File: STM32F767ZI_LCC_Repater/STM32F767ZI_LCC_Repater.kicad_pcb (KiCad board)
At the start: 2 copper layers, 105.6 x 73.3 mm, 6 parts, among them CN10 ST_MORPHO, CN7 ST_MORPHO

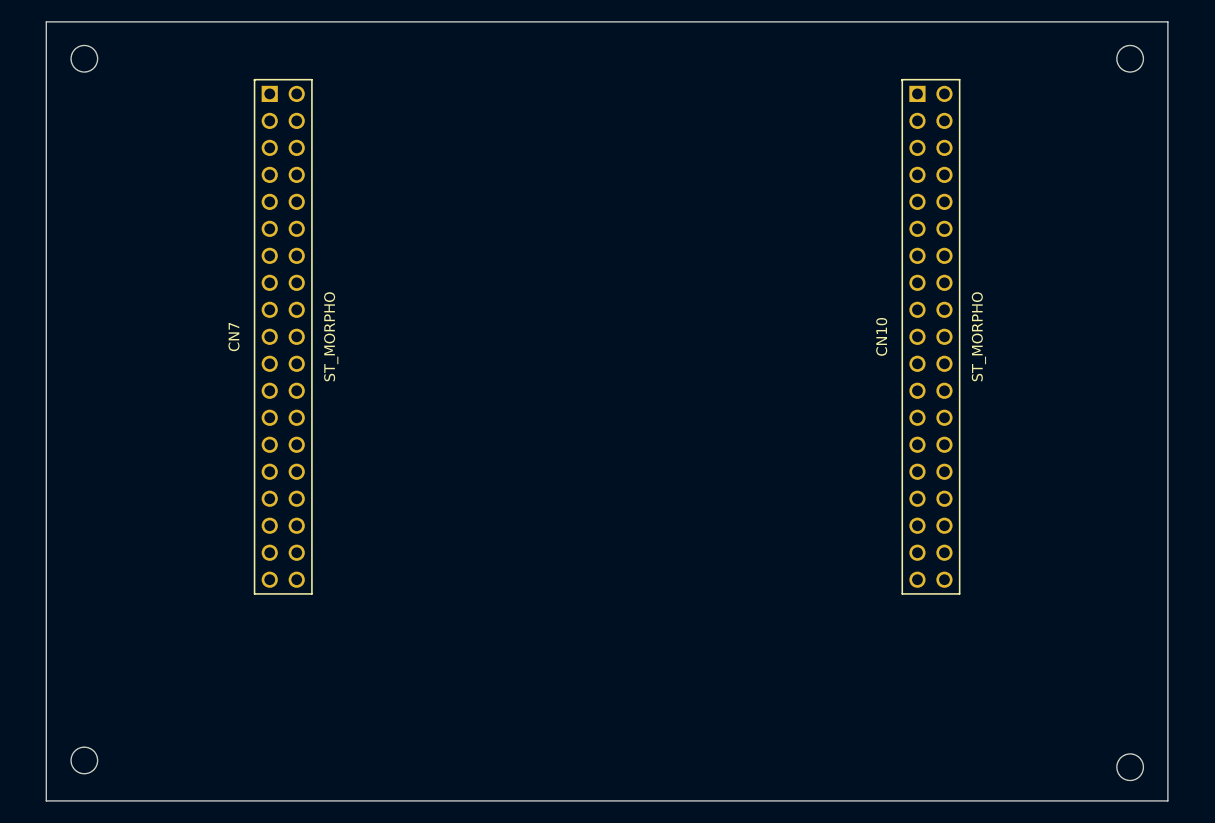
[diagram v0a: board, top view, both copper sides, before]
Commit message: Complete STM32F767ZI_LCC_Repater board.
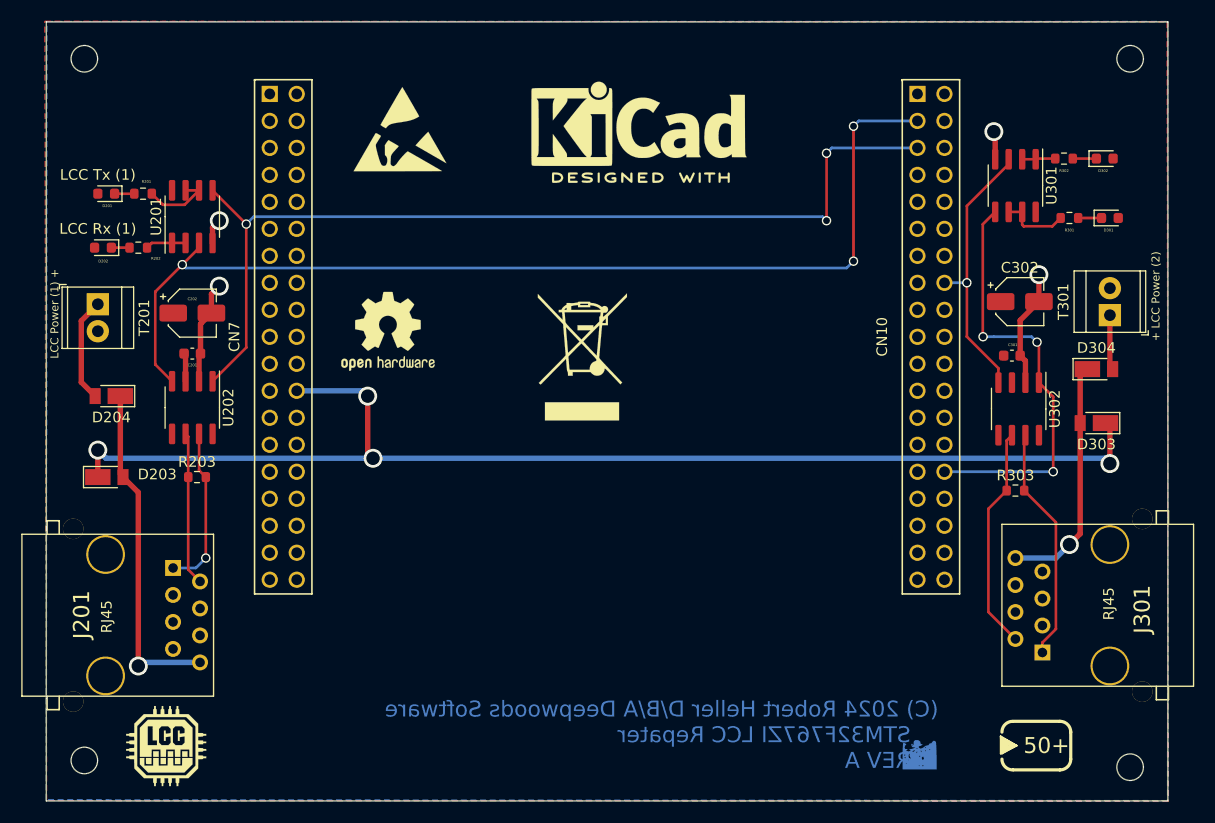
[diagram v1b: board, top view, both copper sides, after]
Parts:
- added C201: .1 uf, Capacitor_SMD:C_0603_1608Metric, F.Cu at (92.7, 191.6)
- added C202: 15 uf 15V, Capacitor_SMD:CP_Elec_4x5.8, F.Cu at (92.7, 187.8)
- added C301: .1 uf, Capacitor_SMD:C_0603_1608Metric, F.Cu at (169.8, 191.8)
- added C302: 15 uf 15V, Capacitor_SMD:CP_Elec_4x5.8, F.Cu at (170.6, 186.7)
- added D201: LCC Tx (1), LED_SMD:LED_0603_1608Metric, F.Cu at (84.6, 176.5)
- added D202: LCC Rx (1), LED_SMD:LED_0603_1608Metric, F.Cu at (84.3, 181.6)
- added D203: SB240, Diode_SMD:D_PowerDI-123, F.Cu at (84.7, 203.2)
- added D204: SB240, Diode_SMD:D_PowerDI-123, F.Cu at (85.1, 195.6)
- added D301: LCC Tx (2), LED_SMD:LED_0603_1608Metric, F.Cu at (179.1, 178.8)
- added D302: LCC Rx (2), LED_SMD:LED_0603_1608Metric, F.Cu at (178.6, 173.2)
- added D303: SB240, Diode_SMD:D_PowerDI-123, F.Cu at (177.8, 198.1)
- added D304: SB240, Diode_SMD:D_PowerDI-123, F.Cu at (177.8, 193.0)
- added G***: LCC, LCCLogo:LCC_LOGO_9x9, F.Cu at (90.3, 228.5)
- added G***: LOGO, DWSLogos:DWSLogoBCU, F.Cu at (161.2, 229.1)
- added J201: RJ45, RJ45:RJ45_8N-S, F.Cu at (84.5, 216.2)
- added J301: RJ45, RJ45:RJ45_8N-S, F.Cu at (179.1, 215.3)
- added R201: 160 Ohms, Resistor_SMD:R_0603_1608Metric, F.Cu at (88.1, 176.5)
- added R202: 160 Ohms, Resistor_SMD:R_0603_1608Metric, F.Cu at (87.6, 181.6)
- added R203: 120, Resistor_SMD:R_0603_1608Metric, F.Cu at (93.2, 203.2)
- added R301: 160 Ohms, Resistor_SMD:R_0603_1608Metric, F.Cu at (175.3, 178.8)
- added R302: 160 Ohms, Resistor_SMD:R_0603_1608Metric, F.Cu at (174.8, 173.2)
- added R303: 120, Resistor_SMD:R_0603_1608Metric, F.Cu at (170.2, 204.5)
- added REF**: ESD-Logo_8.9x8mm_SilkScreen, Symbol:ESD-Logo_8.9x8mm_SilkScreen, F.Cu at (112.3, 170.4)
- added REF**: WEEE-Logo_8.4x12mm_SilkScreen, Symbol:WEEE-Logo_8.4x12mm_SilkScreen, F.Cu at (129.4, 191.9)
- added REF**: KiCad-Logo2_8mm_SilkScreen, Symbol:KiCad-Logo2_8mm_SilkScreen, F.Cu at (134.7, 169.9)
- added REF**: OSHW-Logo2_9.8x8mm_SilkScreen, Symbol:OSHW-Logo2_9.8x8mm_SilkScreen, F.Cu at (111.1, 189.5)
- added REF**: PowerLabel-50Plus, PowerLabels:PowerLabel-50Plus, F.Cu at (173.1, 228.5)
- added T201: LCC Power (1) +, TerminalBlock_TE-Connectivity:TerminalBlock_TE_282834-2_1x02_P2.54mm_Horizontal, F.Cu at (83.8, 186.9)
- added T301: + LCC Power (2), TerminalBlock_TE-Connectivity:TerminalBlock_TE_282834-2_1x02_P2.54mm_Horizontal, F.Cu at (179.1, 188.0)
- added U201: LM358, Package_SO:SOIC-8_3.9x4.9mm_P1.27mm, F.Cu at (92.7, 178.7)
- added U202: TCAN332DR, Package_SO:SOIC-8_3.9x4.9mm_P1.27mm, F.Cu at (92.7, 196.7)
- added U301: LM358, Package_SO:SOIC-8_3.9x4.9mm_P1.27mm, F.Cu at (170.2, 175.8)
- added U302: TCAN332DR, Package_SO:SOIC-8_3.9x4.9mm_P1.27mm, F.Cu at (170.5, 196.8)
- CN10, CN7: footprint ST_Morpho -> STMorpho:ST_Morpho
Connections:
- CN10 pad 1: (no net) -> /PC9
- CN10 pad 10: (no net) -> unconnected-(CN10-Pad10)
- CN10 pad 11: (no net) -> /PA5
- CN10 pad 12: (no net) -> /PA12
- CN10 pad 13: (no net) -> /PA6
- CN10 pad 14: (no net) -> /PA11
- CN10 pad 15: (no net) -> /PA7
- CN10 pad 16: (no net) -> /PB12-CAN2_RX
- CN10 pad 17: (no net) -> /PB6
- CN10 pad 18: (no net) -> /PB11
- CN10 pad 19: (no net) -> /PC7
- CN10 pad 2: (no net) -> /PC8
- CN10 pad 21: (no net) -> /PA9
- CN10 pad 22: (no net) -> /PB2
- CN10 pad 23: (no net) -> /PA8
- CN10 pad 24: (no net) -> /PB1
- CN10 pad 25: (no net) -> /PB10
- CN10 pad 26: (no net) -> /PB15
- CN10 pad 27: (no net) -> /PB4
- CN10 pad 28: (no net) -> /PB14
- CN10 pad 29: (no net) -> /PB5
- CN10 pad 3: (no net) -> /PB8-CAN1_RX
- CN10 pad 30: (no net) -> /PB13-CAN2_TX
- CN10 pad 31: (no net) -> /PB3
- CN10 pad 32: (no net) -> /AGND
- CN10 pad 33: (no net) -> /PA10
- CN10 pad 34: (no net) -> /PC4
- CN10 pad 35: (no net) -> /PA2
- CN10 pad 36: (no net) -> unconnected-(CN10-Pad36)
- CN10 pad 37: (no net) -> /PA3
- CN10 pad 38: (no net) -> unconnected-(CN10-Pad38)
- CN10 pad 4: (no net) -> /PC6
- CN10 pad 5: (no net) -> /PB9-CAN1_TX
- CN10 pad 6: (no net) -> /PC5
- CN10 pad 7: (no net) -> /AVDD
- CN10 pad 8: (no net) -> /U5V
- CN7 pad 1: (no net) -> /PC10
- CN7 pad 10: (no net) -> unconnected-(CN7-Pad10)
- CN7 pad 11: (no net) -> unconnected-(CN7-Pad11)
- CN7 pad 12: (no net) -> /IOREF
- CN7 pad 13: (no net) -> /PA13
- CN7 pad 14: (no net) -> /RESET
- CN7 pad 15: (no net) -> /PA14
- CN7 pad 17: (no net) -> /PA15
- CN7 pad 2: (no net) -> /PC11
- CN7 pad 21: (no net) -> /PB7
- CN7 pad 23: (no net) -> /PC13
- CN7 pad 24: (no net) -> /VIN
- CN7 pad 25: (no net) -> /PC14
- CN7 pad 26: (no net) -> unconnected-(CN7-Pad26)
- CN7 pad 27: (no net) -> /PC15
- CN7 pad 28: (no net) -> /PA0
- CN7 pad 29: (no net) -> /PF0
- CN7 pad 3: (no net) -> /PC12
- CN7 pad 30: (no net) -> /PA1
- CN7 pad 31: (no net) -> /PF1
- CN7 pad 32: (no net) -> /PA4
- CN7 pad 33: (no net) -> /VBAT
- CN7 pad 34: (no net) -> /PB0
- CN7 pad 35: (no net) -> /PC2
- CN7 pad 36: (no net) -> /PC1
- CN7 pad 37: (no net) -> /PC3
- CN7 pad 38: (no net) -> /PC0
- CN7 pad 4: (no net) -> /PD2
- CN7 pad 6: (no net) -> /E5V
- CN7 pad 7: (no net) -> /Boot0
- CN7 pad 9: (no net) -> unconnected-(CN7-Pad9)
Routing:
- net /VIN: track 0.00 -> 115.2 mm, vias 0 -> 4
- net /PB8-CAN1_RX: track 0.00 -> 97.9 mm, vias 0 -> 3
- net /PB9-CAN1_TX: track 0.00 -> 90.8 mm, vias 0 -> 3
- net /PB13-CAN2_TX: track 0.00 -> 40.6 mm, vias 0 -> 3
- net Net-(D203-Pad2): track 0.00 -> 32.0 mm, vias 0 -> 1
- net /PB12-CAN2_RX: track 0.00 -> 26.0 mm, vias 0 -> 1
- net GND: track 0.00 -> 25.9 mm, vias 0 -> 4
- net Net-(D303-Pad2): track 0.00 -> 22.8 mm, vias 0 -> 1
- net Net-(J301-Pad1): track 0.00 -> 22.3 mm
- net Net-(J301-Pad2): track 0.00 -> 21.1 mm
- net Net-(J201-Pad1): track 0.00 -> 15.4 mm, vias 0 -> 1
- net Net-(J201-Pad2): track 0.00 -> 14.5 mm
- net Net-(D204-Pad2): track 0.00 -> 9.83 mm
- net Net-(R201-Pad2): track 0.00 -> 6.71 mm
- net Net-(R301-Pad2): track 0.00 -> 6.48 mm
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- added copper zone on F.Cu, net +3.3V
- added copper zone on B.Cu, net GND
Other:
- board text added: "(C) 2024 Robert Heller D/B/A Deepwoods Software STM32F767ZI LCC Repater REV A"
